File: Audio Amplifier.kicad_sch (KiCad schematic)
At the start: 33 parts, among them J1 AudioJack3, SW1 SW_SPST, U1 TPA3110D2PWP

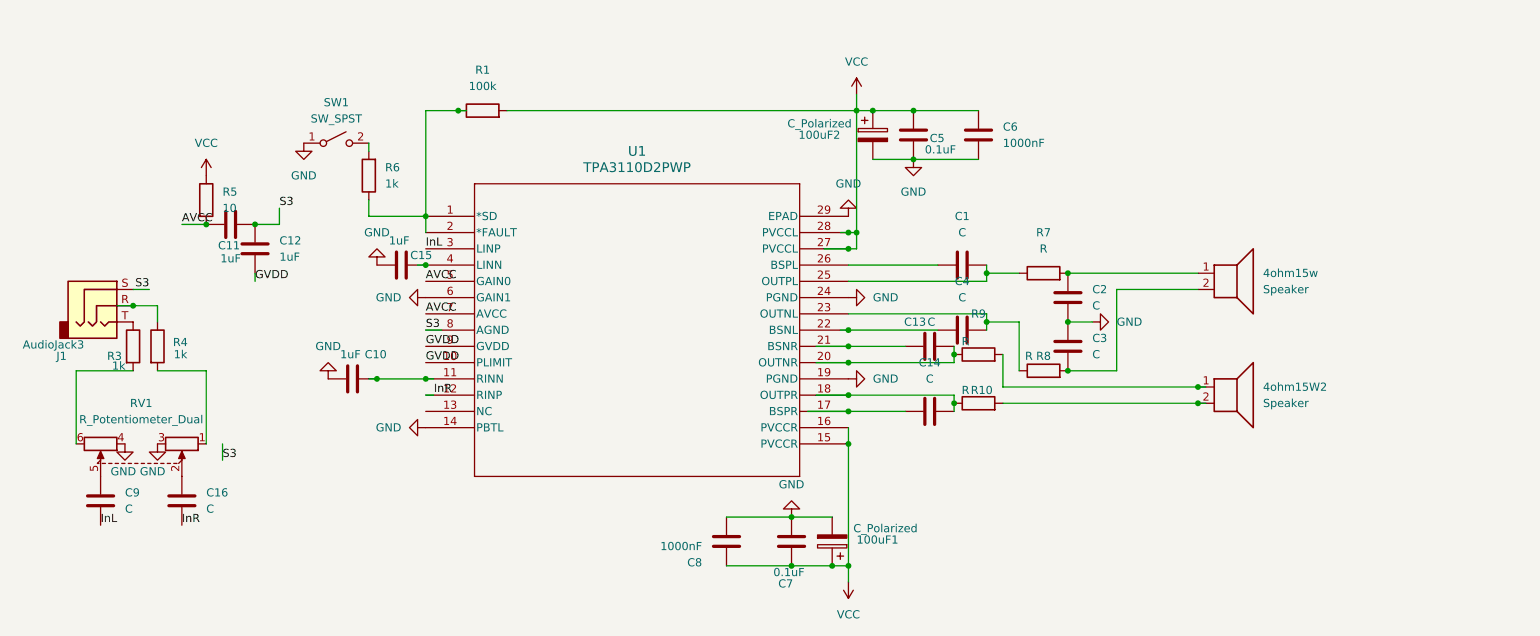
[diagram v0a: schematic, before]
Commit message: Feat(PLIM): Added a voltage divider to the PLIMIT pin on the TPA3110d2. Used 2 10k ohm resistors to provide PLIMIT with 3V.
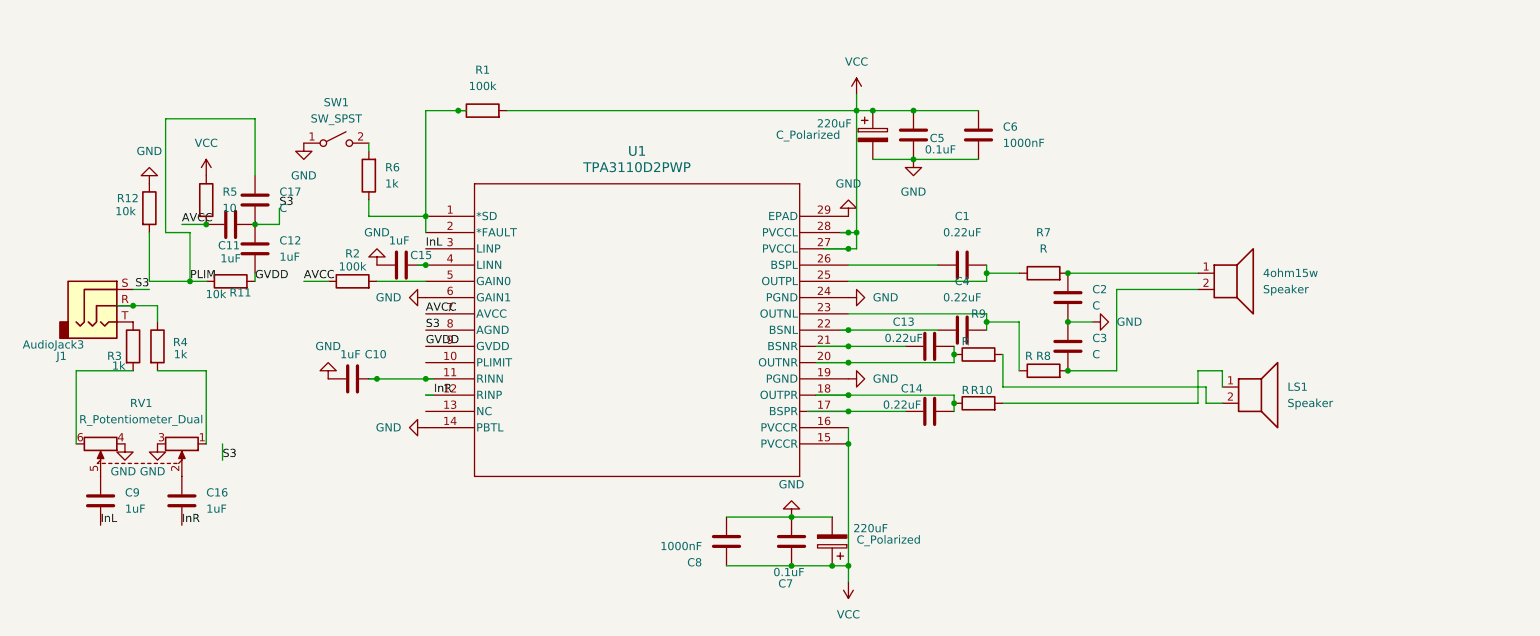
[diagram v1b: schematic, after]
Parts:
- removed 4ohm15W2: Speaker, symbol Device:Speaker
- added C17: C, symbol Device:C
- added LS1: Speaker, symbol Device:Speaker
- added R11, R12: 10k, symbol Device:R
- added R2: 100k, symbol Device:R
- C1, C13, C14, C4: value C -> 0.22uF
- C16, C9: value C -> 1uF
- C_Polarized: renamed from 100uF1; value C_Polarized -> 220uF
- C_Polarized: renamed from 100uF2; value C_Polarized -> 220uF
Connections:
- net AVCC: now also R2.1; no longer U1.5 (GAIN0)
- net GND: now also R12.1
- net GVDD: now also R11.2; no longer U1.10 (PLIMIT)
- net S3: now also C17.2
- net at R10.2: now also LS1.1
- net at R9.2: now also LS1.2
- new net: R2.2, U1.5 (GAIN0)
- new net PLIM: C17.1, R11.1, R12.2

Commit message: Fix(PLIMIT): Connected ground resistor on voltage divider to AGND, connected AGND to GND. Adjusted pullup resistor to 13K to meet desired 3V PLIMIT voltage. Fixed voltage divider capacitor to have a 1uF value.
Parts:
- C17: value C -> 1uF
- R11: value 10k -> 13k
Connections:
- net S3 is gone; now on net GND: C11.2, C12.1, C17.2, J1.S, U1.8 (AGND)
- net PLIM: now also U1.10 (PLIMIT)
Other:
- moved on the sheet: C11, C12, C17, R11, R12, R5

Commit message: Fix(Miscellaneous): Adjusted capacitor values, fixed the potentiometer pins for equal volume control on both sides.
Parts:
- C6, C8: value 1000nF -> 1000pF
- renumbered C_Polarized to C18, C_Polarized to C19
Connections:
- net GND: now also RV1.1; no longer RV1.3
- net at R4.2: now also RV1.3; no longer RV1.1
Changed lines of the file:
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@@
 	(wire
 		(pts
-			(xy 68.58 87.63) (xy 68.58 85.09)
-		)
-		(stroke
-			(width 0)
-			(type default)
-		)
-	)
-	(wire
-		(pts
 			(xy 45.72 73.66) (xy 45.72 85.09)
 		)
@@
 	(wire
 		(pts
-			(xy 58.42 73.66) (xy 66.04 73.66)
-		)
-		(stroke
-			(width 0)
-			(type default)
-		)
-	)
-	(wire
-		(pts
 			(xy 81.28 59.69) (xy 85.09 59.69)
 		)
@@
 	(wire
 		(pts
+			(xy 58.42 73.66) (xy 58.42 85.09)
+		)
+		(stroke
+			(width 0)
+			(type default)
+		)
+	)
+	(wire
+		(pts
 			(xy 167.64 33.02) (xy 167.64 52.07)
 		)
@@
 	(wire
 		(pts
-			(xy 66.04 73.66) (xy 66.04 85.09)
-		)
-		(stroke
-			(width 0)
-			(type default)
-		)
-	)
-	(wire
-		(pts
 			(xy 187.96 58.42) (xy 187.96 59.69)
 		)
@@
 		)
 	)
-	(label "S3"
-		(at 68.58 87.63 0)
-		(effects
-			(font
-				(size 1.27 1.27)
-			)
-			(justify left bottom)
-		)
-	)
 	(label "InL"
 		(at 49.53 97.79 0)
@@
 			)
 		)
-		(property "Value" "1000nF"
+		(property "Value" "1000pF"
 			(at 143.51 101.092 0)
 			(show_name no)
@@
 		(in_pos_files yes)
 		(dnp no)
-		(property "Reference" "C_Polarized"
+		(property "Reference" "C18"
 			(at 167.64 100.076 0)
 			(show_name no)
@@
 			(project "Audio Amplifier"
 				(path "/44284b9d-b892-46b9-bfbe-71e6e2e22151"
-					(reference "C_Polarized")
+					(reference "C18")
 					(unit 1)
 				)
@@
 		(in_pos_files yes)
 		(dnp no)
-		(property "Reference" "C_Polarized"
+		(property "Reference" "C19"
 			(at 165.1 36.83 0)
 			(show_name no)
@@
 			(project "Audio Amplifier"
 				(path "/44284b9d-b892-46b9-bfbe-71e6e2e22151"
-					(reference "C_Polarized")
+					(reference "C19")
 					(unit 1)
 				)
@@
 	)
 	(symbol
+		(lib_id "power:GND")
+		(at 66.04 85.09 0)
+		(unit 1)
+		(body_style 1)
+		(exclude_from_sim no)
+		(in_bom yes)
+		(on_board yes)
+		(in_pos_files yes)
+		(dnp no)
+		(fields_autoplaced yes)
+		(property "Reference" "#PWR015"
+			(at 66.04 91.44 0)
+			(hide yes)
+			(show_name no)
+			(do_not_autoplace no)
+			(effects
+				(font
+					(size 1.27 1.27)
+				)
+			)
+		)
+		(property "Value" "GND"
+			(at 66.04 90.17 0)
+			(show_name no)
+			(do_not_autoplace no)
+			(effects
+				(font
+					(size 1.27 1.27)
+				)
+			)
+		)
+		(property "Footprint" ""
+			(at 66.04 85.09 0)
+			(hide yes)
+			(show_name no)
+			(do_not_autoplace no)
+			(effects
+				(font
+					(size 1.27 1.27)
+				)
+			)
+		)
+		(property "Datasheet" ""
+			(at 66.04 85.09 0)
+			(hide yes)
+			(show_name no)
+			(do_not_autoplace no)
+			(effects
+				(font
+					(size 1.27 1.27)
+				)
+			)
+		)
+		(property "Description" "Power symbol creates a global label with name \"GND\" , ground"
+			(at 66.04 85.09 0)
+			(hide yes)
+			(show_name no)
+			(do_not_autoplace no)
+			(effects
+				(font
+					(size 1.27 1.27)
+				)
+			)
+		)
+		(pin "1"
+		)
+		(instances
+			(project "Audio Amplifier"
+				(path "/44284b9d-b892-46b9-bfbe-71e6e2e22151"
+					(reference "#PWR015")
+					(unit 1)
+				)
+			)
+		)
+	)
+	(symbol
 		(lib_id "Device:R")
 		(at 58.42 48.26 90)
@@
 	)
 	(symbol
-		(lib_id "power:GND")
-		(at 58.42 85.09 0)
-		(unit 1)
-		(body_style 1)
-		(exclude_from_sim no)
-		(in_bom yes)
-		(on_board yes)
-		(in_pos_files yes)
-		(dnp no)
-		(property "Reference" "#PWR015"
-			(at 58.42 91.44 0)
-			(hide yes)
-			(show_name no)
-			(do_not_autoplace no)
-			(effects
-				(font
-					(size 1.27 1.27)
-				)
-			)
-		)
-		(property "Value" "GND"
-			(at 57.658 89.408 0)
-			(show_name no)
-			(do_not_autoplace no)
-			(effects
-				(font
-					(size 1.27 1.27)
-				)
-			)
-		)
-		(property "Footprint" ""
-			(at 58.42 85.09 0)
-			(hide yes)
-			(show_name no)
-			(do_not_autoplace no)
-			(effects
-				(font
-					(size 1.27 1.27)
-				)
-			)
-		)
-		(property "Datasheet" ""
-			(at 58.42 85.09 0)
-			(hide yes)
-			(show_name no)
-			(do_not_autoplace no)
-			(effects
-				(font
-					(size 1.27 1.27)
-				)
-			)
-		)
-		(property "Description" "Power symbol creates a global label with name \"GND\" , ground"
-			(at 58.42 85.09 0)
-			(hide yes)
-			(show_name no)
-			(do_not_autoplace no)
-			(effects
-				(font
-					(size 1.27 1.27)
-				)
-			)
-		)
-		(pin "1"
-		)
-		(instances
-			(project "Audio Amplifier"
-				(path "/44284b9d-b892-46b9-bfbe-71e6e2e22151"
-					(reference "#PWR015")
-					(unit 1)
-				)
-			)
-		)
-	)
-	(symbol
 		(lib_id "Device:C")
 		(at 176.53 36.83 0)
@@
 			)
 		)
-		(property "Value" "1000nF"
+		(property "Value" "1000pF"
 			(at 190.5 38.0999 0)
 			(show_name no)

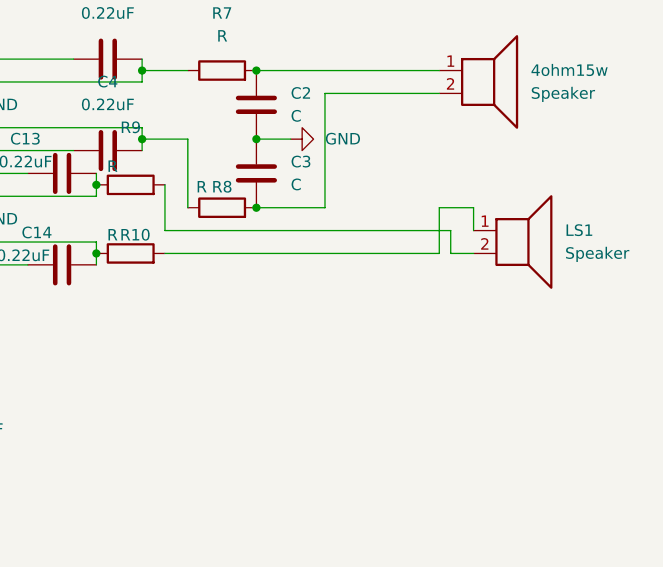
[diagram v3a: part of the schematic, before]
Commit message: Fix(Speaker): Flipped the speaker terminals for less visual clutter.
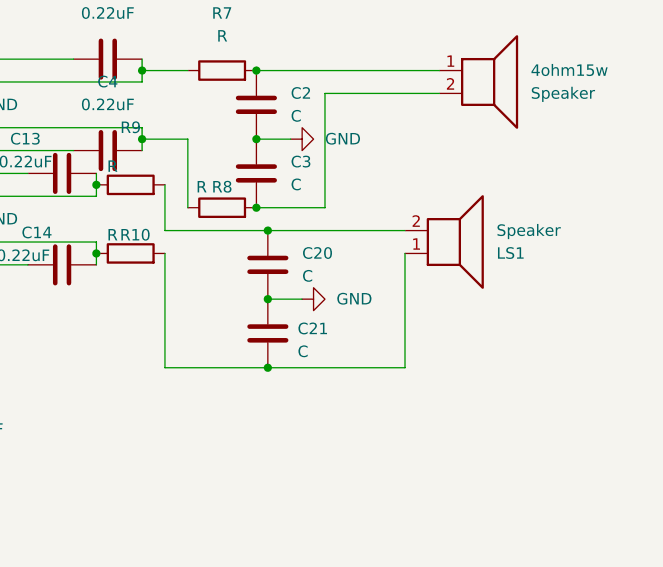
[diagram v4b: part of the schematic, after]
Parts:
- added C20, C21: C, symbol Device:C
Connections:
- net GND: now also C20.2, C21.1
- net at LS1.1, R10.2: now also C21.2
- net at LS1.2, R9.2: now also C20.1
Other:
- moved on the sheet: LS1

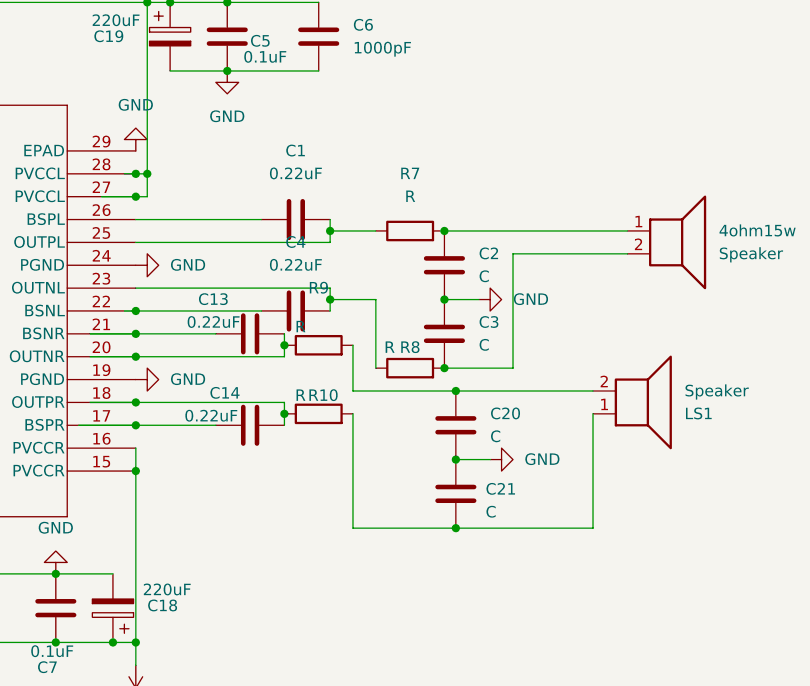
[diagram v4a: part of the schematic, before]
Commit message: Feat(Filter): Swapped the ferrite beads for a dedicated LC filter using 15uH inductor and 2.2uF capacitor.
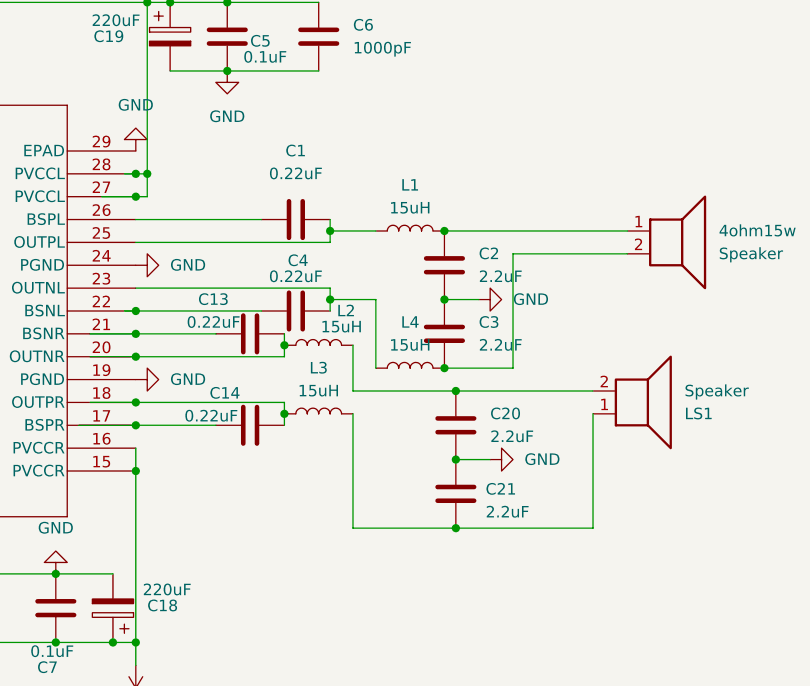
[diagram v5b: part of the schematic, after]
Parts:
- removed R10, R7, R8, R9: R, symbol Device:R
- added L1, L2, L3, L4: 15uH, symbol Device:L
- C2, C20, C21, C3: value C -> 2.2uF
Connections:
- net at C14.2, U1.18 (OUTPR): now also L3.1
- net at C13.2, U1.20 (OUTNR): now also L2.1
- net at C4.2, U1.23 (OUTNL): now also L4.1
- net at C1.2, U1.25 (OUTPL): now also L1.1
- net at 4ohm15w.2, C3.2: now also L4.2
- net at C20.1, LS1.2: now also L2.2
- net at C21.2, LS1.1: now also L3.2
- net at 4ohm15w.1, C2.1: now also L1.2

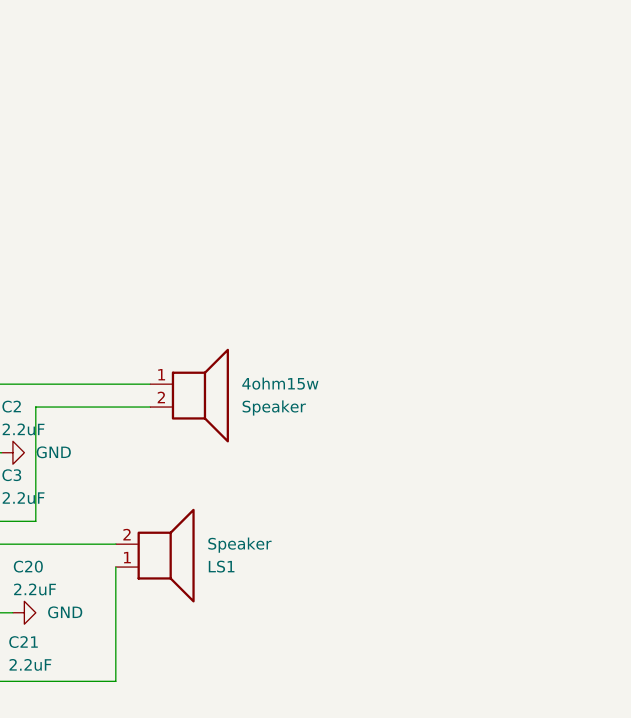
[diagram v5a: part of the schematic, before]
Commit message: Feat(VCC): Added a dedicated connector labeled 12V 5A regulated power supply, and connected it with the VCC net label.
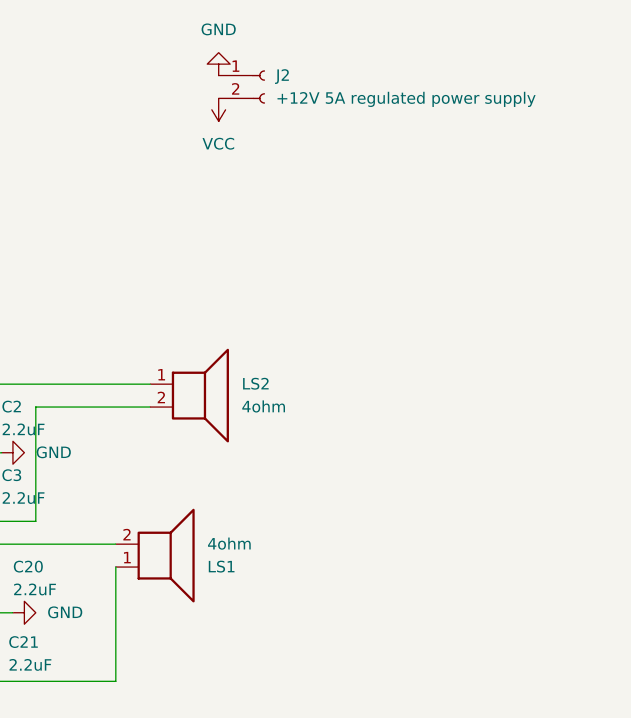
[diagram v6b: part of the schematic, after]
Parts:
- added J2: +12V 5A regulated power supply, symbol Connector:Conn_01x02_Socket
- LS1: value Speaker -> 4ohm
- LS2: renamed from 4ohm15w; value Speaker -> 4ohm
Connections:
- net GND: now also J2.1 (Pin_1)
- net VCC: now also J2.2 (Pin_2)
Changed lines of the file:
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@@
+	)
+	(symbol
+		(lib_id "power:GND")
+		(at 228.6 24.13 180)
+		(unit 1)
+		(body_style 1)
+		(exclude_from_sim no)
+		(in_bom yes)
+		(on_board yes)
+		(in_pos_files yes)
+		(dnp no)
+		(fields_autoplaced yes)
+		(property "Reference" "#PWR019"
+			(at 228.6 17.78 0)
+			(hide yes)
+			(show_name no)
+			(do_not_autoplace no)
+			(effects
+				(font
+					(size 1.27 1.27)
+				)
+			)
+		)
+		(property "Value" "GND"
+			(at 228.6 19.05 0)
+			(show_name no)
+			(do_not_autoplace no)
+			(effects
+				(font
+					(size 1.27 1.27)
+				)
+			)
+		)
+		(property "Footprint" ""
+			(at 228.6 24.13 0)
+			(hide yes)
+			(show_name no)
+			(do_not_autoplace no)
+			(effects
+				(font
+					(size 1.27 1.27)
+				)
+			)
+		)
+		(property "Datasheet" ""
+			(at 228.6 24.13 0)
+			(hide yes)
+			(show_name no)
+			(do_not_autoplace no)
+			(effects
+				(font
+					(size 1.27 1.27)
+				)
+			)
+		)
+		(property "Description" "Power symbol creates a global label with name \"GND\" , ground"
+			(at 228.6 24.13 0)
+			(hide yes)
+			(show_name no)
+			(do_not_autoplace no)
+			(effects
+				(font
+					(size 1.27 1.27)
+				)
+			)
+		)
+		(pin "1"
+		)
+		(instances
+			(project "Audio Amplifier"
+				(path "/44284b9d-b892-46b9-bfbe-71e6e2e22151"
+					(reference "#PWR019")
+					(unit 1)
+				)
+			)
+		)
 	)
 	(symbol
@@
 			)
 		)
-		(property "Value" "Speaker"
+		(property "Value" "4ohm"
 			(at 227.33 76.2001 0)
 			(show_name no)
@@
 	)
 	(symbol
+		(lib_id "power:VCC")
+		(at 228.6 26.67 180)
+		(unit 1)
+		(body_style 1)
+		(exclude_from_sim no)
+		(in_bom yes)
+		(on_board yes)
+		(in_pos_files yes)
+		(dnp no)
+		(fields_autoplaced yes)
+		(property "Reference" "#PWR020"
+			(at 228.6 22.86 0)
+			(hide yes)
+			(show_name no)
+			(do_not_autoplace no)
+			(effects
+				(font
+					(size 1.27 1.27)
+				)
+			)
+		)
+		(property "Value" "VCC"
+			(at 228.6 31.75 0)
+			(show_name no)
+			(do_not_autoplace no)
+			(effects
+				(font
+					(size 1.27 1.27)
+				)
+			)
+		)
+		(property "Footprint" ""
+			(at 228.6 26.67 0)
+			(hide yes)
+			(show_name no)
+			(do_not_autoplace no)
+			(effects
+				(font
+					(size 1.27 1.27)
+				)
+			)
+		)
+		(property "Datasheet" ""
+			(at 228.6 26.67 0)
+			(hide yes)
+			(show_name no)
+			(do_not_autoplace no)
+			(effects
+				(font
+					(size 1.27 1.27)
+				)
+			)
+		)
+		(property "Description" "Power symbol creates a global label with name \"VCC\""
+			(at 228.6 26.67 0)
+			(hide yes)
+			(show_name no)
+			(do_not_autoplace no)
+			(effects
+				(font
+					(size 1.27 1.27)
+				)
+			)
+		)
+		(pin "1"
+		)
+		(instances
+			(project "Audio Amplifier"
+				(path "/44284b9d-b892-46b9-bfbe-71e6e2e22151"
+					(reference "#PWR020")
+					(unit 1)
+				)
+			)
+		)
+	)
+	(symbol
 		(lib_id "Connector_Audio:AudioJack3")
 		(at 49.53 63.5 0)
@@
 		(dnp no)
 		(fields_autoplaced yes)
-		(property "Reference" "4ohm15w"
+		(property "Reference" "LS2"
 			(at 231.14 58.4199 0)
 			(show_name no)
@@
 			)
 		)
-		(property "Value" "Speaker"
+		(property "Value" "4ohm"
 			(at 231.14 60.9599 0)
 			(show_name no)
@@
 			(project "Audio Amplifier"
 				(path "/44284b9d-b892-46b9-bfbe-71e6e2e22151"
-					(reference "4ohm15w")
+					(reference "LS2")
 					(unit 1)
 				)
@@
 					(unit 1)
 				)
+			)
+		)
+	)
+	(symbol
+		(lib_id "Connector:Conn_01x02_Socket")
+		(at 233.68 24.13 0)
+		(unit 1)
+		(body_style 1)
+		(exclude_from_sim no)
+		(in_bom yes)
+		(on_board yes)
+		(in_pos_files yes)
+		(dnp no)
+		(fields_autoplaced yes)
+		(property "Reference" "J2"
+			(at 234.95 24.1299 0)
+			(show_name no)
+			(do_not_autoplace no)
+			(effects
+				(font
+					(size 1.27 1.27)
+				)
+				(justify left)
+			)
+		)
+		(property "Value" "+12V 5A regulated power supply"
+			(at 234.95 26.6699 0)
+			(show_name no)
+			(do_not_autoplace no)
+			(effects
+				(font
+					(size 1.27 1.27)
+				)
+				(justify left)
+			)
+		)
+		(property "Footprint" ""
+			(at 233.68 24.13 0)
+			(hide yes)
+			(show_name no)
+			(do_not_autoplace no)
+			(effects
+				(font
+					(size 1.27 1.27)
+				)
+			)
+		)
+		(property "Datasheet" ""
+			(at 233.68 24.13 0)
+			(hide yes)
+			(show_name no)
+			(do_not_autoplace no)
+			(effects
+				(font
+					(size 1.27 1.27)
+				)
+			)
+		)
+		(property "Description" "Generic connector, single row, 01x02, script generated"
+			(at 233.68 24.13 0)
+			(hide yes)
+			(show_name no)
+			(do_not_autoplace no)
+			(effects
+				(font
+					(size 1.27 1.27)
+				)
+			)
+		)
+		(pin "1"
+		)
+		(pin "2"
+		)
+		(instances
+			(project "Audio Amplifier"
+				(path "/44284b9d-b892-46b9-bfbe-71e6e2e22151"
+					(reference "J2")
+					(unit 1)
+				)
